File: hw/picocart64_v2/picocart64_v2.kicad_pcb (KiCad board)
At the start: 4 copper layers, 100 x 60 mm, 122 parts, among them J1 USB_C_Receptacle_USB2.0, J2 Conn_02x06_Odd_Even, J3 Micro_SD_Card_Det, Q1 FDN340P, Q2 FDN340P, SW1 BootButton, SW2 ResetButton, U1 APS6404L-3SQR, U10 W25Q128JVS, U11 74LVC1G125GW, U13 AZ1117-3.3, U14 N64-Cartridge, U15 RP2040, U16 RP2040, U17 ESP32-C3-WROOM-02, U2 APS6404L-3SQR, U3 APS6404L-3SQR, U4 APS6404L-3SQR, U5 APS6404L-3SQR, U6 APS6404L-3SQR, U7 APS6404L-3SQR, U8 APS6404L-3SQR, U9 SN74LVC138AQDRQ1, Y1 12MHz 10ppm, Y2 12MHz 10ppm

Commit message: Updated hardware files
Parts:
- added C39: 1u, Capacitor_SMD:C_0402_1005Metric, F.Cu at (114.6, 96.7)
- added C40: 1u, Capacitor_SMD:C_0402_1005Metric, F.Cu at (136.7, 96.7)
- added C41: 1u, Capacitor_SMD:C_0402_1005Metric, F.Cu at (128.9, 96.7)
- added C42: 1u, Capacitor_SMD:C_0402_1005Metric, F.Cu at (115.5, 84.6)
- added C43: 1u, Capacitor_SMD:C_0402_1005Metric, F.Cu at (131.1, 84.6)
- added C44: 1u, Capacitor_SMD:C_0402_1005Metric, F.Cu at (139.2, 84.1)
- added C45: 1u, Capacitor_SMD:C_0402_1005Metric, F.Cu at (121.2, 96.7)
- added C46: 1u, Capacitor_SMD:C_0402_1005Metric, F.Cu at (123.3, 84.6)
- added C47: 1u, Capacitor_SMD:C_0402_1005Metric, F.Cu at (144.5, 96.8)
- added C48: 100n, Capacitor_SMD:C_0402_1005Metric, F.Cu at (158.7, 84.5)
- added C49: 100n, Capacitor_SMD:C_0402_1005Metric, F.Cu at (161.6, 91.1)
- added C50: 100n, Capacitor_SMD:C_0402_1005Metric, F.Cu at (157.4, 85.8)
- added C51: 100n, Capacitor_SMD:C_0402_1005Metric, F.Cu at (164.6, 85.1)
- added C52: 100n, Capacitor_SMD:C_0402_1005Metric, F.Cu at (163.3, 83.8)
- added C53: 100n, Capacitor_SMD:C_0402_1005Metric, F.Cu at (149.7, 76.3)
- added C54: 100n, Capacitor_SMD:C_0402_1005Metric, F.Cu at (149.3, 80.5)
- added C55: 100n, Capacitor_SMD:C_0402_1005Metric, F.Cu at (137.4, 82.0)
- added C56: 100n, Capacitor_SMD:C_0402_1005Metric, F.Cu at (137.4, 80.2)
- added C57: 100n, Capacitor_SMD:C_0402_1005Metric, F.Cu at (149.3, 78.5)
- added R42: R, Resistor_SMD:R_0402_1005Metric, F.Cu at (143.5, 80.1)
- added R43: R, Resistor_SMD:R_0402_1005Metric, F.Cu at (162.8, 87.9)
- added R44: R, Resistor_SMD:R_0402_1005Metric, F.Cu at (143.5, 81.0)
- added R45: R, Resistor_SMD:R_0402_1005Metric, F.Cu at (162.1, 87.3)
- added R46: R, Resistor_SMD:R_0402_1005Metric, F.Cu at (145.4, 81.0)
- added R47: R, Resistor_SMD:R_0402_1005Metric, F.Cu at (161.0, 86.6)
- added R48: R, Resistor_SMD:R_0402_1005Metric, F.Cu at (145.4, 80.1)
- added R49: R, Resistor_SMD:R_0402_1005Metric, F.Cu at (160.4, 86.0)
- added R50: R, Resistor_SMD:R_0402_1005Metric, F.Cu at (146.1, 76.7)
- added R51: R, Resistor_SMD:R_0402_1005Metric, F.Cu at (160.4, 89.0)
- added R52: R, Resistor_SMD:R_0402_1005Metric, F.Cu at (146.1, 75.8)
- added R53: R, Resistor_SMD:R_0402_1005Metric, F.Cu at (161.0, 89.7)
- added R54: R, Resistor_SMD:R_0402_1005Metric, F.Cu at (145.7, 78.9)
- added R55: R, Resistor_SMD:R_0402_1005Metric, F.Cu at (159.1, 87.3)
- added R56: R, Resistor_SMD:R_0402_1005Metric, F.Cu at (145.7, 77.9)
- added R57: R, Resistor_SMD:R_0402_1005Metric, F.Cu at (159.7, 87.9)
- added R58: R, Resistor_SMD:R_0402_1005Metric, F.Cu at (143.2, 77.9)
- added R59: R, Resistor_SMD:R_0402_1005Metric, F.Cu at (164.6, 89.2)
- added R60: R, Resistor_SMD:R_0402_1005Metric, F.Cu at (143.2, 78.9)
- added R61: R, Resistor_SMD:R_0402_1005Metric, F.Cu at (163.9, 88.5)
- added R62: 10K, Resistor_SMD:R_0402_1005Metric, F.Cu at (150.3, 97.5)
- moved U8 27.4 mm to (137.8, 93.5), turned to 180 degrees
- moved U5 25.3 mm to (114.5, 93.5), turned to 180 degrees
- moved R39 22.1 mm to (151.3, 97.5), turned to -90 degrees
- moved C9 11.7 mm to (142.6, 96.8), turned to 0 degrees
- moved U7 10.00 mm to (130.0, 93.5), turned to 180 degrees
- moved C8 9.80 mm to (134.9, 96.7), turned to 0 degrees
- moved U11 9.77 mm to (153.4, 97.0), turned to 180 degrees
- moved C7 8.05 mm to (127.1, 96.7), turned to 0 degrees
- moved U6 7.96 mm to (122.2, 93.5), turned to 180 degrees
- moved C5 6.48 mm to (119.4, 96.7), turned to 0 degrees
- moved J3 5.50 mm to (198.4, 67.8)
- moved C2 5.26 mm to (111.6, 96.7), turned to 0 degrees
- moved U4 4.12 mm to (114.5, 87.8)
- moved U10 3.85 mm to (146.4, 93.5), turned to 180 degrees
- moved C1 3.25 mm to (117.4, 84.6)
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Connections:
- U2 pad 1: /PSRAM Array/CS1 -> /PSRAM Array/CS2
- U3 pad 1: /PSRAM Array/CS1 -> /PSRAM Array/CS3
- U4 pad 1: /PSRAM Array/CS1 -> /PSRAM Array/CS4
- U5 pad 1: /PSRAM Array/CS1 -> /PSRAM Array/CS5
- U6 pad 1: /PSRAM Array/CS1 -> /PSRAM Array/CS6
- U7 pad 1: /PSRAM Array/CS1 -> /PSRAM Array/CS7
- U8 pad 1: /PSRAM Array/CS1 -> /PSRAM Array/CS8
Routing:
- net /PSRAM Array/CS1: track 251.2 -> 63.1 mm
- net /Mainboard/SSI_SD1: track 0.00 -> 132.2 mm, vias 0 -> 2
- net /Mainboard/SSI_SD2: track 0.00 -> 128.6 mm, vias 0 -> 2
- net /Mainboard/SSI_SCLK: track 236.3 -> 131.5 mm, vias 6 -> 0
- net +3V3: track 117.3 -> 218.3 mm, vias 36 -> 51
- net /Mainboard/SSI_SD3: track 232.8 -> 132.0 mm, vias 6 -> 2
- net Net-(R39-Pad2): track 32.4 -> 102.0 mm
- net GND: track 196.0 -> 265.6 mm, vias 89 -> 93
- net /PSRAM Array/CS5: track 0.00 -> 63.0 mm
- net /PSRAM Array/CS2: track 0.00 -> 62.9 mm
- net /PSRAM Array/CS7: track 0.00 -> 62.9 mm
- net /Mainboard/CIC_DCLK: track 48.4 -> 88.1 mm
- net /Mainboard/CIC_DIO: track 50.6 -> 90.1 mm
- net /Mainboard/~{NMI}: track 48.4 -> 87.7 mm
- net /Mainboard/~{COLD_RESET}: track 137.3 -> 176.4 mm
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- added copper zone on In1.Cu, net +3V3
- added copper zone on In1.Cu, net /Mainboard/VBUS'
- added copper zone on In2.Cu, net GND
- removed copper zone on In2.Cu, net +3V3
- removed copper zone on In2.Cu, net /Mainboard/VBUS'
- removed copper zone on In1.Cu, net GND
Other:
- board size 100 x 60 mm -> 105 x 60 mm
- board text added: "REV. B"
- board text removed: "REV. A"

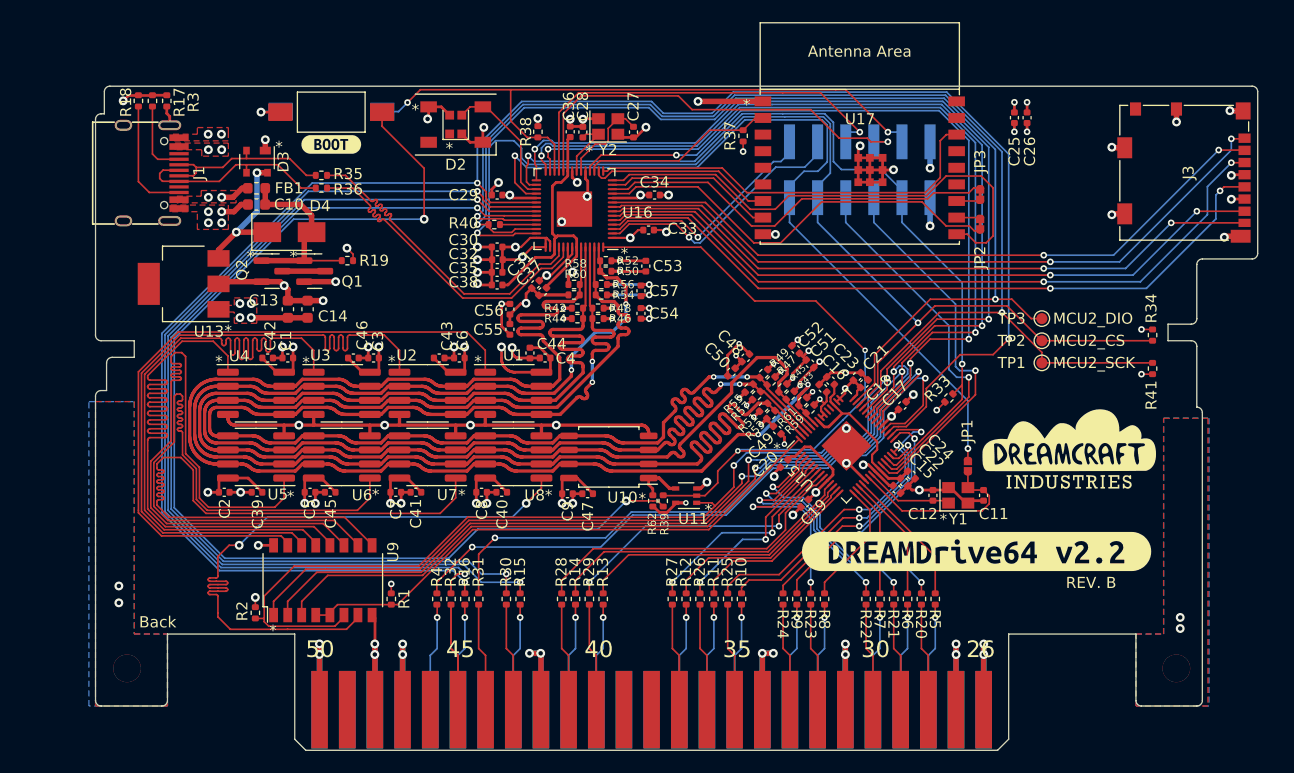
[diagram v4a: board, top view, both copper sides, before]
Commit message: Updated schematic to include a chin for the USB port and slightly increased the length of the SD Card chin. This should help it be more accessible once inside a shell. Updated schematic to include part numbers for all the components.
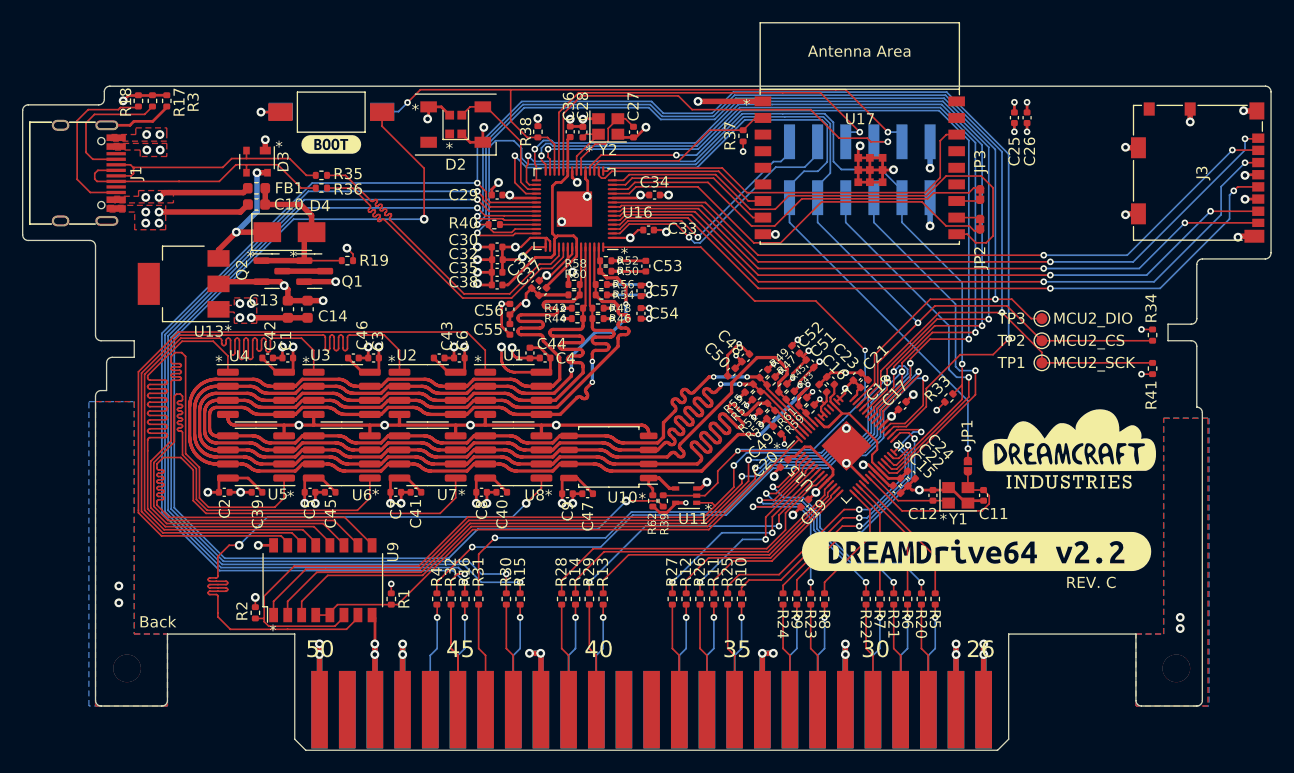
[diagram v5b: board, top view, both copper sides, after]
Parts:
- added G***: LOGO, LOGO, B.Cu at (113.5, 91.8)
- moved J1 5.68 mm to (98.7, 67.9)
- moved J3 1.24 mm to (199.6, 67.8)
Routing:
- net /Mainboard/MCU2_USB_D-: track 16.1 -> 22.0 mm
- net /Mainboard/MCU2_USB_D+: track 18.9 -> 24.8 mm
- net GND: track 265.6 -> 271.3 mm
- net /Mainboard/VBUS': track 2.88 -> 8.37 mm
- net Net-(J1-PadA5): track 6.86 -> 12.3 mm
- net Net-(J1-PadB5): track 10.8 -> 15.4 mm
- net Net-(J1-PadS1): track 1.80 -> 6.16 mm
- net /Mainboard/SD_DAT0: track 62.0 -> 63.3 mm
- net /Mainboard/SD_CLK: track 65.1 -> 66.3 mm
- net /Mainboard/SD_DAT3: track 63.0 -> 64.3 mm
- net /Mainboard/SD_DAT1: track 61.2 -> 62.4 mm
- net /Mainboard/SD_DAT2: track 64.5 -> 65.7 mm
- net /Mainboard/SD_CMD: track 65.8 -> 67.0 mm
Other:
- board size 105 x 60 mm -> 112.8 x 60 mm
- board text added: "REV. C"
- board text removed: "REV. B"
